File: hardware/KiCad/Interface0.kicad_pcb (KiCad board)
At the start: 2 copper layers, 75 x 85 mm, 7 parts, among them J1 RPi_GPIO

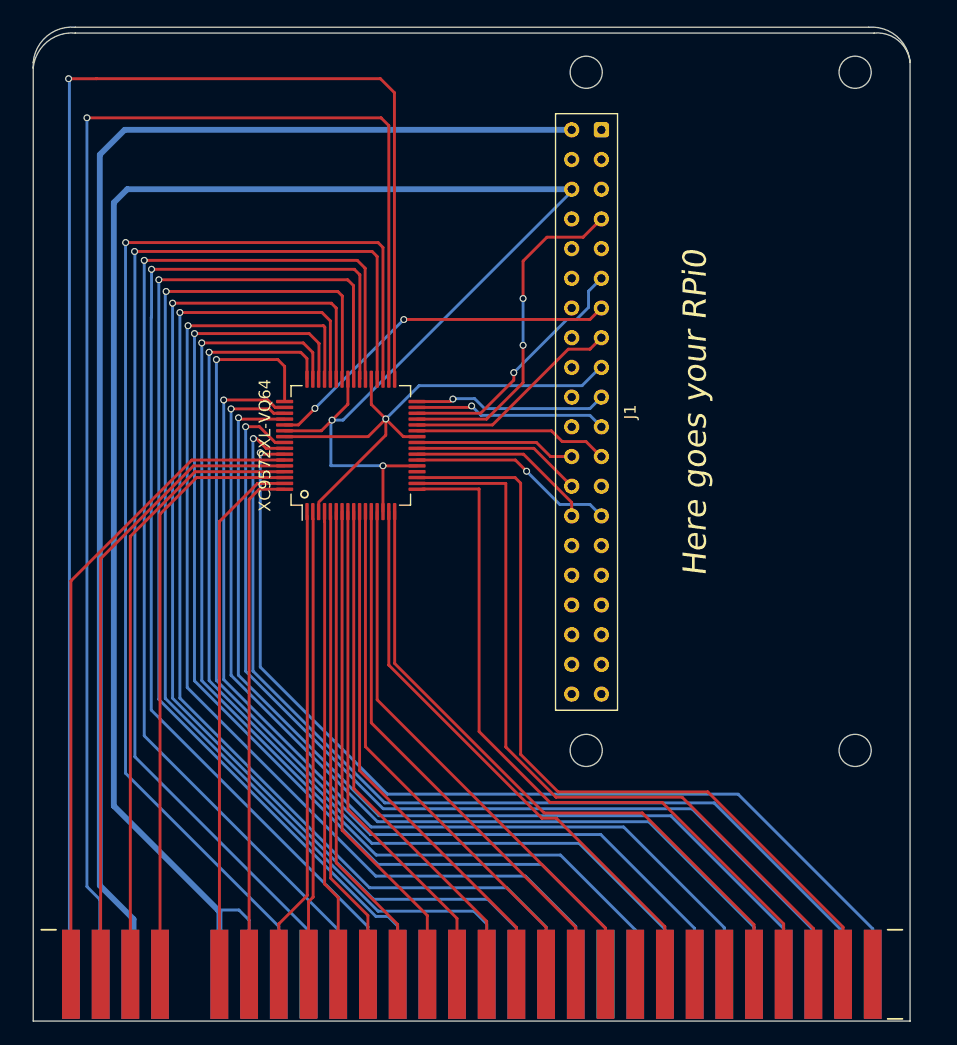
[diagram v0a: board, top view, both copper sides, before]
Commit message: Incorporate Álvaro Lopes tips
- connect MREQ/IOREQ & SPI_CLK to GCKx
- connect RESET to GSR
- restucture the other pins to make it cleaner
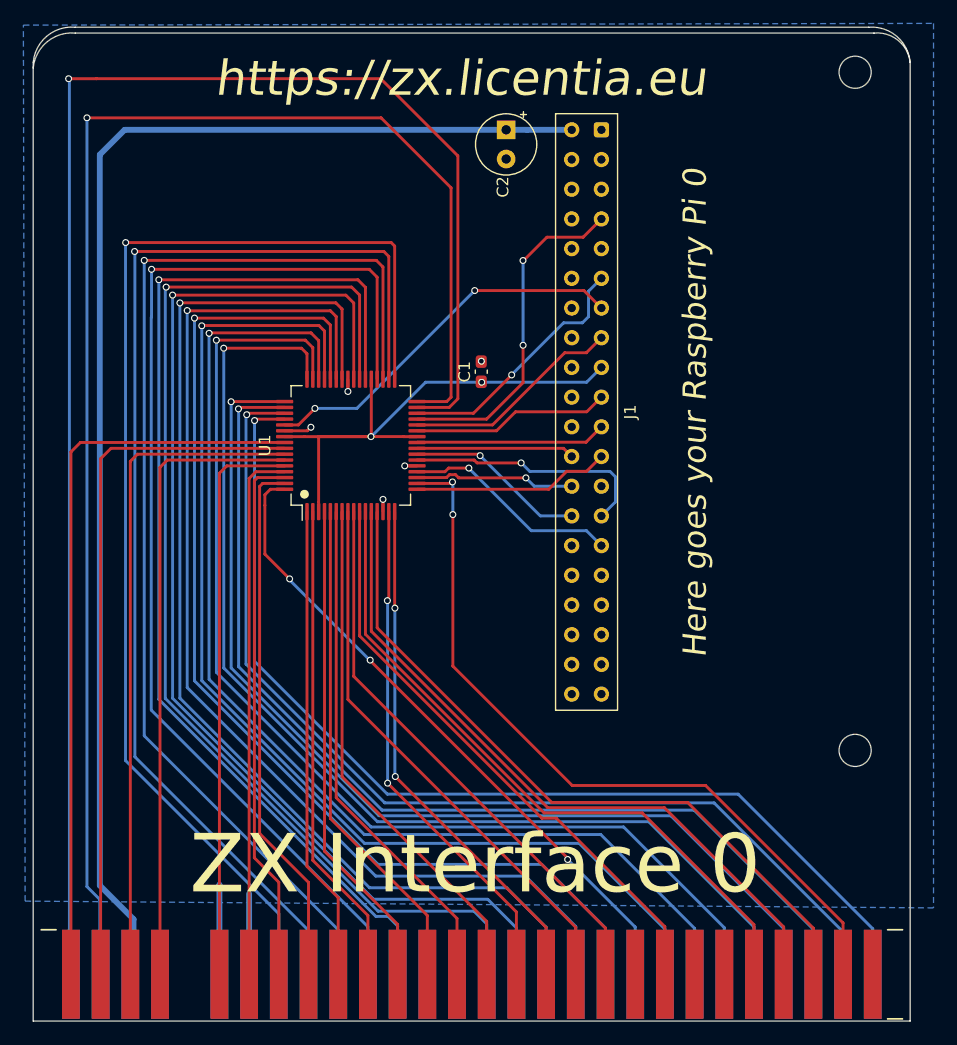
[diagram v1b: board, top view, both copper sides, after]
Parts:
- removed the ? at (68.3, 77.5)
- removed the ? at (68.3, 19.5)
- added C1: 22uF, Capacitor_SMD:C_0603_1608Metric_Pad1.08x0.95mm_HandSolder, F.Cu at (59.3, 45.1)
- added C2: 100nF, Capacitor_THT:CP_Radial_Tantal_D5.0mm_P2.50mm, F.Cu at (61.5, 24.4)
- renumbered XC9572XL-VQ64 to U1
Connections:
- J1 pad 29: unconnected-(J1-Pad29) -> /GPIO1
- J1 pad 30: unconnected-(J1-Pad30) -> GND
- J1 pad 34: unconnected-(J1-Pad34) -> GND
- J1 pad 39: unconnected-(J1-Pad39) -> GND
- U1 pad 1: /D2 -> /D5
- U1 pad 10: /MREQ -> /WAIT
- U1 pad 11: /IORQ -> /M1
- U1 pad 12: /RD -> /RFSH
- U1 pad 13: /WR -> /A8
- U1 pad 15: /WAIT -> /MREQ
- U1 pad 16: /M1 -> /IORQ
- U1 pad 17: /RFSH -> /SPI_CLK
- U1 pad 18: /A8 -> /A10
- U1 pad 19: /A10 -> /GPIO4
- U1 pad 2: /D6 -> /D3
- U1 pad 24: /GPIO4 -> /SPI_CE0
- U1 pad 25: /SPI_CE0 -> /SPI_MISO
- U1 pad 27: /SPI_CLK -> /SPI_MOSI
- U1 pad 31: /SPI_MISO -> /A14
- U1 pad 32: /SPI_MOSI -> /A12
- U1 pad 33: /A14 -> /CLK
- U1 pad 34: /A12 -> /A0
- U1 pad 35: /CLK -> /A1
- U1 pad 36: /A0 -> /A2
- U1 pad 38: /A1 -> /A3
- U1 pad 39: /A2 -> /ROMCS2
- U1 pad 4: /D5 -> /D4
- U1 pad 40: /A3 -> /DRD
- U1 pad 42: /ROMCS2 -> /DWR
- U1 pad 43: /DRD -> /MTR
- U1 pad 44: /DWR -> /BUSRQ
- U1 pad 45: /MTR -> /A7
- U1 pad 46: /BUSRQ -> /A6
- U1 pad 47: /RESET -> /A5
- U1 pad 48: /A7 -> /A4
- U1 pad 49: /A6 -> /ROMCS
- U1 pad 5: /D3 -> /INT
- U1 pad 50: /A5 -> /BUSACK
- U1 pad 51: /A4 -> /A9
- U1 pad 52: /ROMCS -> /A11
- U1 pad 56: /BUSACK -> /A15
- U1 pad 57: /A9 -> /A13
- U1 pad 58: /A11 -> /D7
- U1 pad 59: /A15 -> /ROMCS1
- U1 pad 6: /D4 -> /NMI
- U1 pad 60: /A13 -> /D0
- U1 pad 61: /D7 -> /D1
- U1 pad 62: /ROMCS1 -> /D2
- U1 pad 63: /D0 -> /D6
- U1 pad 64: /D1 -> /RESET
- U1 pad 7: /INT -> /HALT
- U1 pad 8: /NMI -> /RD
- U1 pad 9: /HALT -> /WR
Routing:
- net GND: track 169.6 -> 20.1 mm, vias 2 -> 5
- net /RESET: track 90.7 -> 56.0 mm, vias 1 -> 3
- net /GPIO1: track 0.00 -> 18.7 mm, vias 0 -> 1
- net /A5: track 85.0 -> 96.1 mm
- net /A4: track 85.2 -> 95.4 mm
- net /A14: track 128.0 -> 135.7 mm
- net /A7: track 90.1 -> 97.4 mm
- net /A15: track 56.2 -> 63.3 mm
- net /A12: track 119.9 -> 126.7 mm
- net /A6: track 90.1 -> 96.8 mm
- net /D6: track 39.1 -> 45.7 mm
- net /A13: track 54.6 -> 60.2 mm
- net /D2: track 40.2 -> 45.8 mm
- net /A8: track 66.8 -> 61.8 mm
- net /BUSRQ: track 90.9 -> 95.4 mm
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- added copper zone on B.Cu, net GND
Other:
- board text added: "Here goes your Raspberry Pi 0"
- board text added: "https://zx.licentia.eu"
- board text removed: "Here goes your RPi0"

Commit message: Prepare for first release
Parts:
- added ?: , , F.Cu at (33.1, 29.3)
- added ?: , , F.Cu at (61.0, 67.1)
- C1: footprint Capacitor_SMD:C_0603_1608Metric_Pad1.08x0.95mm_HandSolder -> Capacitor_THT:CP_Radial_Tantal_D7.0mm_P2.50mm
- moved C1 0.98 mm to (58.9, 46.0)
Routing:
- net GND: vias 5 -> 4
- net +3V3: vias 2 -> 1
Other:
- board text added: "ZX Interface0 v3.1"
- board text removed: "ZX Interface 0"
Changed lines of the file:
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@@
   (title_block
     (title "Interface0")
-    (rev "3")
+    (date "2022-05-02")
+    (rev "3.1")
+    (company "https://zx.licentia.eu")
+    (comment 1 "Raspberry PI 0 (2) based ZX Interface")
   )
   (layers
@@
       (drillshape 0)
       (scaleselection 1)
-      (outputdirectory "meta/")
+      (outputdirectory "Interface0/")
     )
   )
@@
   (net 87 "unconnected-(J1-Pad25)")
   (net 88 "unconnected-(J1-Pad9)")
+  (footprint "" (layer "F.Cu")
+    (at 33.094 29.308 90)
+    (fp_text reference "" (at 0 0 90) (layer "F.SilkS")
+      (effects (font (size 1.27 1.27) (thickness 0.15)))
+    )
+    (fp_text value "" (at 0 0 90) (layer "F.SilkS")
+      (effects (font (size 1.27 1.27) (thickness 0.15)))
+    )
+    (pad "" np_thru_hole circle locked (at 0 0 90) (size 2.75 2.75) (drill 2.75) (layers *.Cu *.Mask)
+      (solder_mask_margin 1.725) (clearance 1.725))
+  )
   (footprint "Capacitor_THT:CP_Radial_Tantal_D5.0mm_P2.50mm" (layer "F.Cu")
     (at 61.45 24.38 -90)
@@
     )
   )
-  (footprint "Capacitor_SMD:C_0603_1608Metric_Pad1.08x0.95mm_HandSolder" (layer "F.Cu")
-    (at 59.32 45.07 90)
-    (descr "Capacitor SMD 0603 (1608 Metric), square (rectangular) end terminal, IPC_7351 nominal with elongated pad for handsoldering. (Body size source: IPC-SM-782 page 76, https://www.pcb-3d.com/wordpress/wp-content/uploads/ipc-sm-782a_amendment_1_and_2.pdf), generated with kicad-footprint-generator")
-    (tags "capacitor handsolder")
+  (footprint "Capacitor_THT:CP_Radial_Tantal_D7.0mm_P2.50mm" (layer "F.Cu")
+    (at 58.947 45.976139 90)
+    (descr "CP, Radial_Tantal series, Radial, pin pitch=2.50mm, , diameter=7.0mm, Tantal Electrolytic Capacitor, http://cdn-reichelt.de/documents/datenblatt/B300/TANTAL-TB-Serie%23.pdf")
+    (tags "CP Radial_Tantal series Radial pin pitch 2.50mm  diameter 7.0mm Tantal Electrolytic Capacitor")
     (property "Sheetfile" "Interface0.kicad_sch")
     (property "Sheetname" "")
-    (attr smd)
-    (fp_text reference "C1" (at 0 -1.43 90) (layer "F.SilkS")
-      (effects (font (size 1 1) (thickness 0.15)))
-    )
-    (fp_text value "22uF" (at 0 1.43 90) (layer "F.Fab")
-      (effects (font (size 1 1) (thickness 0.15)))
-    )
-    (fp_text user "${REFERENCE}" (at 0 0 90) (layer "F.Fab")
-      (effects (font (size 0.4 0.4) (thickness 0.06)))
-    )
-    (fp_line (start -0.146267 -0.51) (end 0.146267 -0.51) (layer "F.SilkS") (width 0.12))
-    (fp_line (start -0.146267 0.51) (end 0.146267 0.51) (layer "F.SilkS") (width 0.12))
-    (fp_line (start -1.65 0.73) (end -1.65 -0.73) (layer "F.CrtYd") (width 0.05))
-    (fp_line (start -1.65 -0.73) (end 1.65 -0.73) (layer "F.CrtYd") (width 0.05))
-    (fp_line (start 1.65 -0.73) (end 1.65 0.73) (layer "F.CrtYd") (width 0.05))
-    (fp_line (start 1.65 0.73) (end -1.65 0.73) (layer "F.CrtYd") (width 0.05))
-    (fp_line (start -0.8 -0.4) (end 0.8 -0.4) (layer "F.Fab") (width 0.1))
-    (fp_line (start -0.8 0.4) (end -0.8 -0.4) (layer "F.Fab") (width 0.1))
-    (fp_line (start 0.8 -0.4) (end 0.8 0.4) (layer "F.Fab") (width 0.1))
-    (fp_line (start 0.8 0.4) (end -0.8 0.4) (layer "F.Fab") (width 0.1))
-    (pad "1" smd roundrect (at -0.8625 0 90) (size 1.075 0.95) (layers "F.Cu" "F.Paste" "F.Mask") (roundrect_rratio 0.25)
+    (attr through_hole)
+    (fp_text reference "C1" (at 1.25 -4.75 90) (layer "F.SilkS")
+      (effects (font (size 1 1) (thickness 0.15)))
+    )
+    (fp_text value "22uF" (at 1.25 4.75 90) (layer "F.Fab")
+      (effects (font (size 1 1) (thickness 0.15)))
+    )
+    (fp_text user "${REFERENCE}" (at 1.25 0 90) (layer "F.Fab")
+      (effects (font (size 1 1) (thickness 0.15)))
+    )
+    (fp_line (start -2.274723 -2.385) (end -2.274723 -1.685) (layer "F.SilkS") (width 0.12))
+    (fp_line (start -2.624723 -2.035) (end -1.924723 -2.035) (layer "F.SilkS") (width 0.12))
+    (fp_circle (center 1.25 0) (end 4.87 0) (layer "F.SilkS") (width 0.12) (fill none))
+    (fp_circle (center 1.25 0) (end 5 0) (layer "F.CrtYd") (width 0.05) (fill none))
+    (fp_line (start -1.745708 -1.5275) (end -1.045708 -1.5275) (layer "F.Fab") (width 0.1))
+    (fp_line (start -1.395708 -1.8775) (end -1.395708 -1.1775) (layer "F.Fab") (width 0.1))
+    (fp_circle (center 1.25 0) (end 4.75 0) (layer "F.Fab") (width 0.1) (fill none))
+    (pad "1" thru_hole rect (at 0 0 90) (size 1.6 1.6) (drill 0.8) (layers *.Cu *.Mask)
       (net 1 "+3V3") (pintype "passive"))
-    (pad "2" smd roundrect (at 0.8625 0 90) (size 1.075 0.95) (layers "F.Cu" "F.Paste" "F.Mask") (roundrect_rratio 0.25)
+    (pad "2" thru_hole circle (at 2.5 0 90) (size 1.6 1.6) (drill 0.8) (layers *.Cu *.Mask)
       (net 4 "GND") (pintype "passive"))
-    (model "${KICAD6_3DMODEL_DIR}/Capacitor_SMD.3dshapes/C_0603_1608Metric.wrl"
+    (model "${KICAD6_3DMODEL_DIR}/Capacitor_THT.3dshapes/CP_Radial_Tantal_D7.0mm_P2.50mm.wrl"
       (offset (xyz 0 0 0))
       (scale (xyz 1 1 1))
       (rotate (xyz 0 0 0))
     )
+  )
+  (footprint "" (layer "F.Cu")
+    (at 60.978 67.118 90)
+    (fp_text reference "" (at 0 0 90) (layer "F.SilkS")
+      (effects (font (size 1.27 1.27) (thickness 0.15)))
+    )
+    (fp_text value "" (at 0 0 90) (layer "F.SilkS")
+      (effects (font (size 1.27 1.27) (thickness 0.15)))
+    )
+    (pad "" np_thru_hole circle locked (at 0 0 90) (size 2.75 2.75) (drill 2.75) (layers *.Cu *.Mask)
+      (solder_mask_margin 1.725) (clearance 1.725))
   )
   (footprint "Package_QFP:TQFP-64_10x10mm_P0.5mm" (layer "F.Cu")
@@
   (gr_line (start 24.596 15.609) (end 92.456 15.609) (layer "Edge.Cuts") (width 0.1))
   (gr_line (start 21 100.609) (end 96 100.609) (layer "Edge.Cuts") (width 0.1))
-  (gr_text "ZX Interface 0" (at 56.45 20) (layer "B.SilkS")
-    (effects (font (size 5 5) (thickness 0.75)) (justify mirror))
+  (gr_text "ZX Interface0 v3.1" (at 56.45 20) (layer "B.SilkS")
+    (effects (font (size 4 4) (thickness 0.75)) (justify mirror))
   )
   (gr_text "https://zx.licentia.eu" (at 90.75 48.15 90) (layer "B.SilkS")
     (effects (font (size 3 3) (thickness 0.5) italic) (justify mirror))
   )
-  (gr_text "ZX Interface 0" (at 58.8 87.2) (layer "F.SilkS")
-    (effects (font (size 5 5) (thickness 0.75)))
+  (gr_text "ZX Interface0 v3.1" (at 58.8 87.2) (layer "F.SilkS")
+    (effects (font (size 4 4) (thickness 0.75)))
   )
   (gr_text "Here goes your Raspberry Pi 0" (at 77.6 48.6 90) (layer "F.SilkS")
@@
   (segment (start 49.89 50.62) (end 45.41 50.62) (width 0.25) (layer "F.Cu") (net 1))
   (via (at 49.89 50.62) (size 0.6) (drill 0.4) (layers "F.Cu" "B.Cu") (net 1))
-  (via (at 59.36 45.97) (size 0.6) (drill 0.4) (layers "F.Cu" "B.Cu") (net 1))
   (segment (start 59.36 45.97) (end 59.67 45.97) (width 0.25) (layer "B.Cu") (net 1))
   (segment (start 68.33 45.97) (end 69.596 44.704) (width 0.25) (layer "B.Cu") (net 1))
@@
   (segment (start 50.91522 57.037347) (end 50.91522 55.988291) (width 0.25) (layer "F.Cu") (net 4))
   (via (at 52.778664 53.124847) (size 0.6) (drill 0.4) (layers "F.Cu" "B.Cu") (net 4))
-  (via (at 59.33 44.17) (size 0.6) (drill 0.4) (layers "F.Cu" "B.Cu") (net 4))
   (via (at 44.75 49.82) (size 0.6) (drill 0.4) (layers "F.Cu" "B.Cu") (net 4))
   (via (at 47.91522 46.761403) (size 0.6) (drill 0.4) (layers "F.Cu" "B.Cu") (net 4))

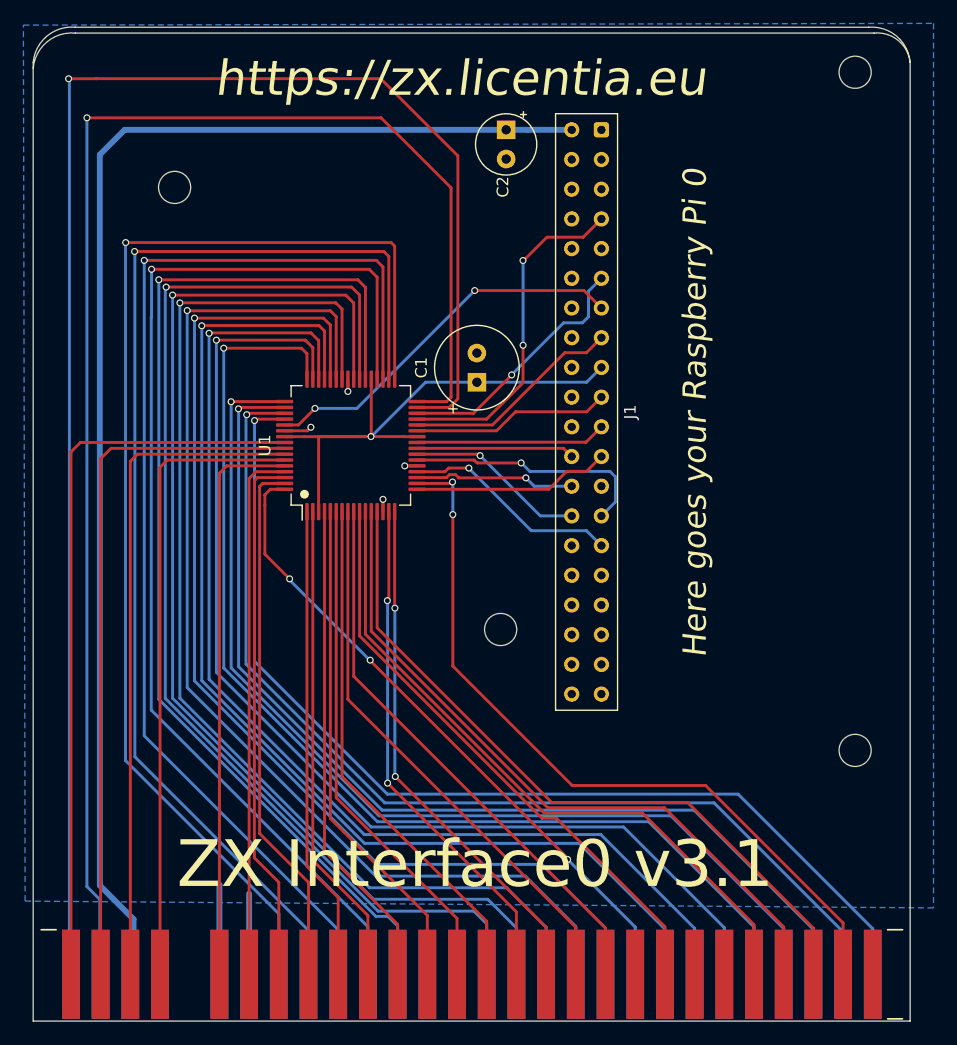
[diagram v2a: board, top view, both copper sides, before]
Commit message: PI_CE0 acts as a clock and we must wire it to a clock pin
Wire the Z80 CPU clock to the remaing one.
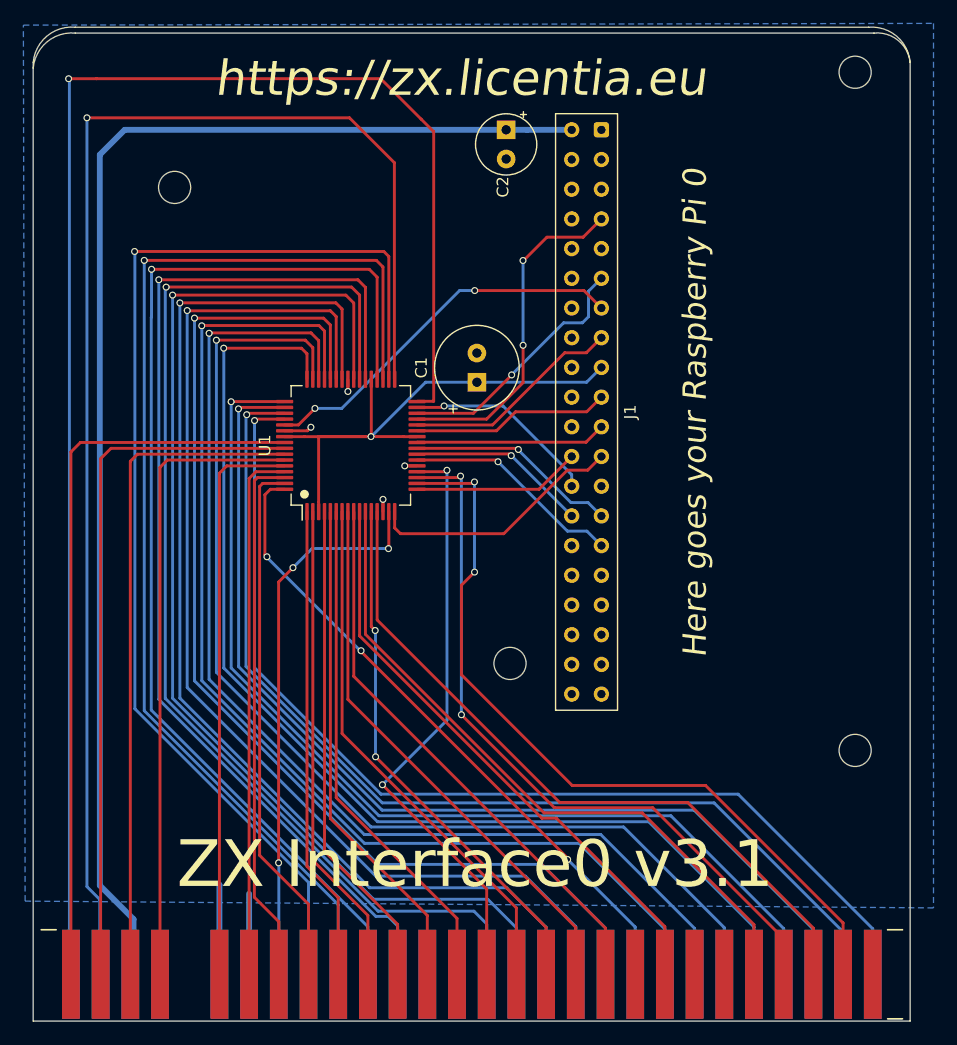
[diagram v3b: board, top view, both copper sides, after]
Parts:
- moved ? 3.01 mm to (61.8, 70.0)
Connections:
- U1 pad 12: /RFSH -> /IORQ
- U1 pad 15: /MREQ -> /CLK
- U1 pad 16: /IORQ -> /SPI_CLK
- U1 pad 17: /SPI_CLK -> /SPI_CE0
- U1 pad 19: /GPIO4 -> /RFSH
- U1 pad 20: /GPIO1 -> /HALT
- U1 pad 22: /GPIO2 -> /GPIO1
- U1 pad 24: /SPI_CE0 -> /GPIO2
- U1 pad 31: /A14 -> /GPIO4
- U1 pad 32: /A12 -> /A14
- U1 pad 33: /CLK -> /A12
- U1 pad 7: /HALT -> /MREQ
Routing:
- net /CLK: track 102.5 -> 47.3 mm, vias 1 -> 3
- net /A12: track 126.7 -> 118.5 mm
- net /HALT: track 44.7 -> 51.7 mm, vias 0 -> 2
- net /SPI_CLK: track 16.9 -> 22.0 mm
- net /GPIO2: track 21.4 -> 18.2 mm
- net /A14: track 135.7 -> 132.7 mm
- net /GPIO4: track 13.7 -> 16.7 mm
- net /RFSH: track 60.0 -> 62.8 mm, vias 0 -> 2
- net /A10: track 65.7 -> 67.7 mm
- net /MREQ: track 44.2 -> 45.7 mm, vias 2 -> 0
- net /SPI_CE0: track 13.5 -> 14.4 mm
- net /IORQ: track 44.9 -> 45.8 mm
- net /GPIO3: track 15.4 -> 14.7 mm
